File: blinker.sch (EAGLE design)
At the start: 13 parts, among them U1 ATTINY85-20S, U2 L3GD20H, U3 MIC5504-3.3YM5-T5

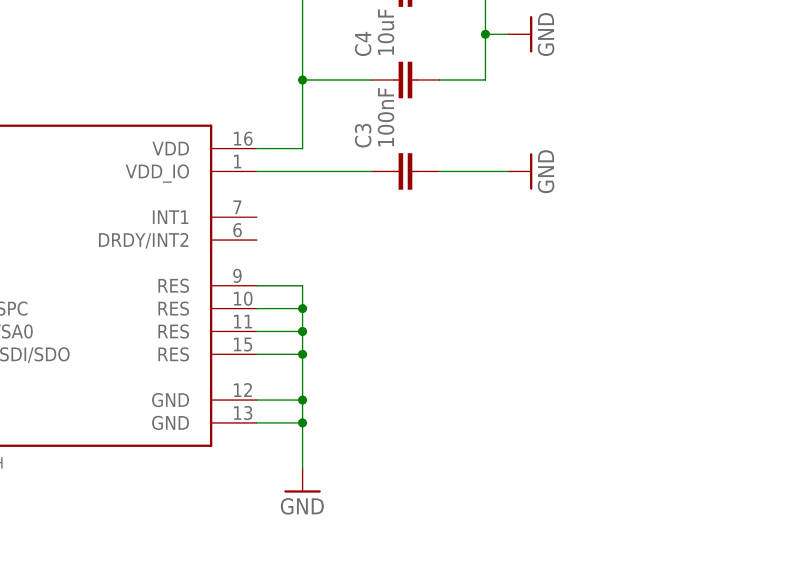
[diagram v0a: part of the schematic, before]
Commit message: fix gyro connections
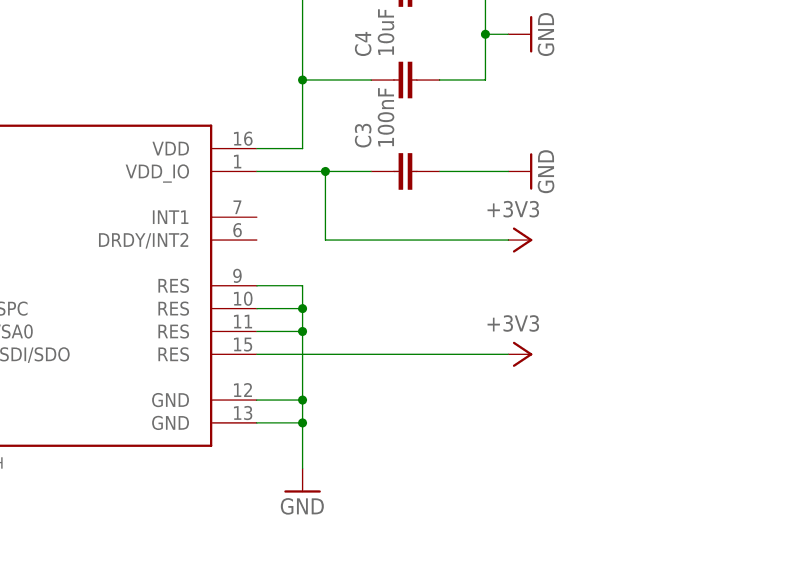
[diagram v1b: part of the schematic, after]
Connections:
- removed net N$2: C3.1, U2.VDD_IO
- net +3V3: now also C3.1, U2.RES@4, U2.VDD_IO
- net GND: no longer U2.RES@4
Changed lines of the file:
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@@
 <part name="C1" library="Capacitor" library_urn="urn:adsk.eagle:library:16290819" deviceset="C" device="CHIP-1206(3216-METRIC)" package3d_urn="urn:adsk.eagle:package:16290893/2" technology="_" value="1uF"/>
 <part name="LEDS" library="pinhead" library_urn="urn:adsk.eagle:library:325" deviceset="PINHD-1X5" device="/90" package3d_urn="urn:adsk.eagle:package:22467/2"/>
+<part name="+3V4" library="supply1" library_urn="urn:adsk.eagle:library:371" deviceset="+3V3" device=""/>
+<part name="+3V5" library="supply1" library_urn="urn:adsk.eagle:library:371" deviceset="+3V3" device=""/>
 </parts>
 <sheets>
@@
 <attribute name="NAME" x="-11.43" y="107.315" size="1.778" layer="95"/>
 <attribute name="VALUE" x="-11.43" y="88.9" size="1.778" layer="96"/>
+</instance>
+<instance part="+3V4" gate="G$1" x="114.3" y="73.66" smashed="yes" rot="R270">
+<attribute name="VALUE" x="109.22" y="76.2" size="1.778" layer="96"/>
+</instance>
+<instance part="+3V5" gate="G$1" x="114.3" y="86.36" smashed="yes" rot="R270">
+<attribute name="VALUE" x="109.22" y="88.9" size="1.778" layer="96"/>
 </instance>
 </instances>
@@
 <pinref part="U2" gate="G$1" pin="RES@2"/>
 <wire x1="88.9" y1="78.74" x2="88.9" y2="76.2" width="0.1524" layer="91"/>
-<wire x1="88.9" y1="76.2" x2="88.9" y2="73.66" width="0.1524" layer="91"/>
-<wire x1="88.9" y1="73.66" x2="88.9" y2="68.58" width="0.1524" layer="91"/>
+<wire x1="88.9" y1="76.2" x2="88.9" y2="68.58" width="0.1524" layer="91"/>
 <wire x1="83.82" y1="78.74" x2="88.9" y2="78.74" width="0.1524" layer="91"/>
 <junction x="88.9" y="78.74"/>
@@
 <wire x1="83.82" y1="76.2" x2="88.9" y2="76.2" width="0.1524" layer="91"/>
 <junction x="88.9" y="76.2"/>
-<pinref part="U2" gate="G$1" pin="RES@4"/>
-<wire x1="83.82" y1="73.66" x2="88.9" y2="73.66" width="0.1524" layer="91"/>
-<junction x="88.9" y="73.66"/>
 </segment>
 <segment>
@@
 <pinref part="C4" gate="G$1" pin="1"/>
 </segment>
+<segment>
+<pinref part="U2" gate="G$1" pin="RES@4"/>
+<wire x1="83.82" y1="73.66" x2="111.76" y2="73.66" width="0.1524" layer="91"/>
+<pinref part="+3V4" gate="G$1" pin="+3V3"/>
+</segment>
+<segment>
+<pinref part="U2" gate="G$1" pin="VDD_IO"/>
+<wire x1="83.82" y1="93.98" x2="91.44" y2="93.98" width="0.1524" layer="91"/>
+<pinref part="C3" gate="G$1" pin="1"/>
+<wire x1="91.44" y1="93.98" x2="96.52" y2="93.98" width="0.1524" layer="91"/>
+<wire x1="91.44" y1="93.98" x2="91.44" y2="86.36" width="0.1524" layer="91"/>
+<junction x="91.44" y="93.98"/>
+<wire x1="91.44" y1="86.36" x2="111.76" y2="86.36" width="0.1524" layer="91"/>
+<pinref part="+3V5" gate="G$1" pin="+3V3"/>
+</segment>
 </net>
 <net name="N$1" class="0">
@@
 </segment>
 </net>
-<net name="N$2" class="0">
-<segment>
-<pinref part="U2" gate="G$1" pin="VDD_IO"/>
-<wire x1="83.82" y1="93.98" x2="96.52" y2="93.98" width="0.1524" layer="91"/>
-<pinref part="C3" gate="G$1" pin="1"/>
-</segment>
-</net>
